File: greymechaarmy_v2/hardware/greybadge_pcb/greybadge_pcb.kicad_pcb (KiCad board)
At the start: 2 copper layers, 75 x 99 mm, 150 parts, among them J1 Conn_02x05_Row_Letter_First, J2 Conn_02x05_Row_Letter_First, J3 Conn_02x05_Row_Letter_First, J4 JST PH S2B, J5 USB_C_Receptacle_USB2.0, Q1 2N7002, Q2 Q_NMOS_GSD, SW1 SW_Push, SW10 SW_Push, SW2 SW_Push, SW3 SW_Push, SW4 SW_Push, SW5 SW_Push, SW6 SW_Push, SW7 SW_Push, SW8 SW_SPDT, SW9 SW_Push, U10 AMS1117-3.3, U2 TLV73311PDBV, U3 TLV73325PDBV, U4 GC9A01_IPS_display, U5 BQ24075, U6 W25Q128JVS, U7 RP2350_60QFN, U8 ECP5U_25_CABGA256, U9 W25Q128JVSIM, X1 SiT2001B, Y1 12Mhz

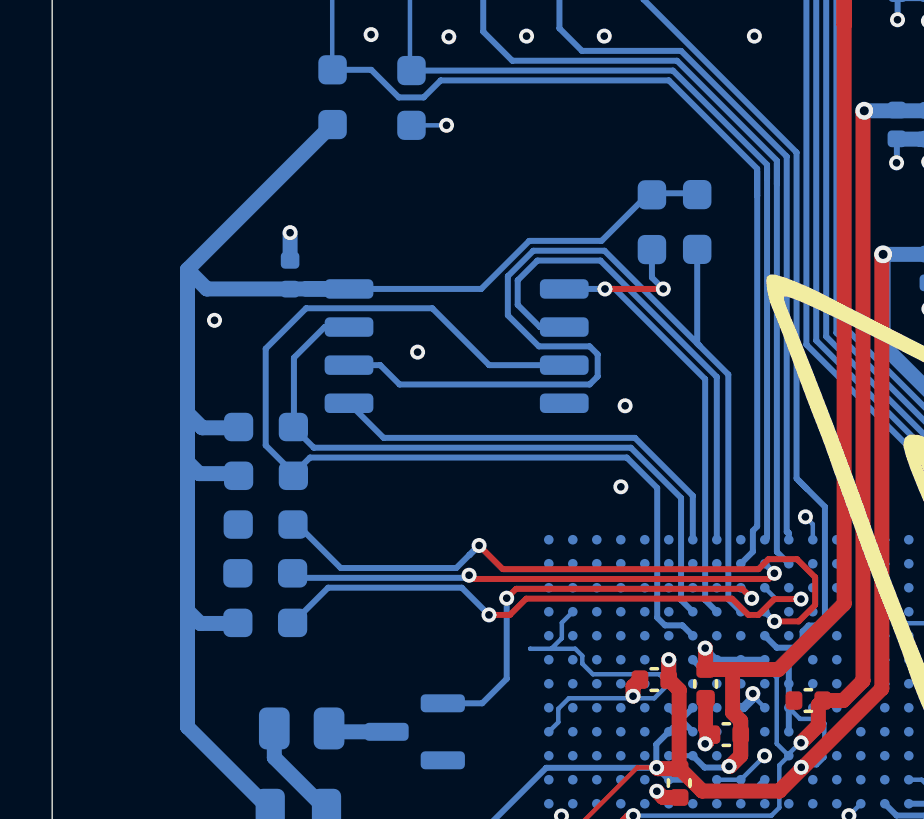
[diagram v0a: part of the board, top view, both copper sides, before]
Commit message: fix: spi flash pinout
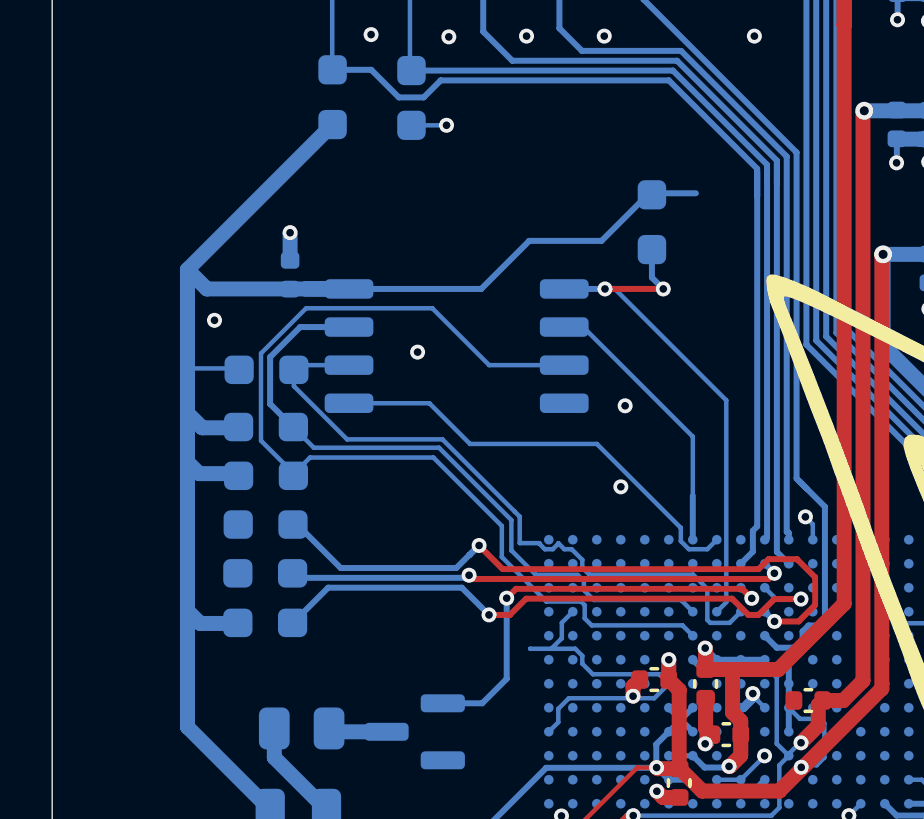
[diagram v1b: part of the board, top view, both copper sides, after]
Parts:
- moved R40 15.2 mm to (88.9, 76.3), turned to 180 degrees
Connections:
- U9 pad 2: sdo -> sdi
- U9 pad 5: sdi -> sdo
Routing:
- net sd_clk: track 35.0 -> 22.2 mm
- net sdi: track 14.2 -> 9.23 mm
- net sdo: track 16.6 -> 14.7 mm
- net +3V3: track 363.3 -> 365.1 mm
- net sd_io2: track 34.4 -> 32.8 mm

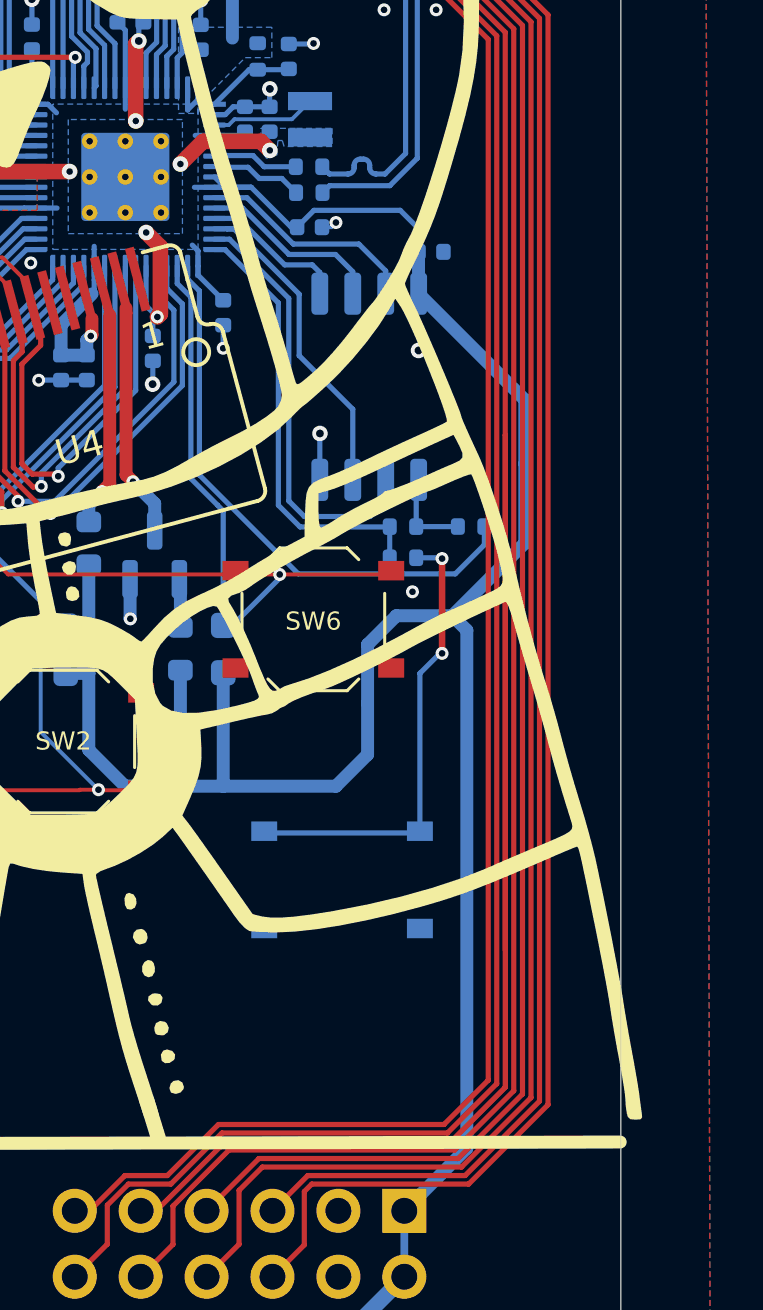
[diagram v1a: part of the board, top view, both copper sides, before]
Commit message: feat: greymecha psram addition in PCB
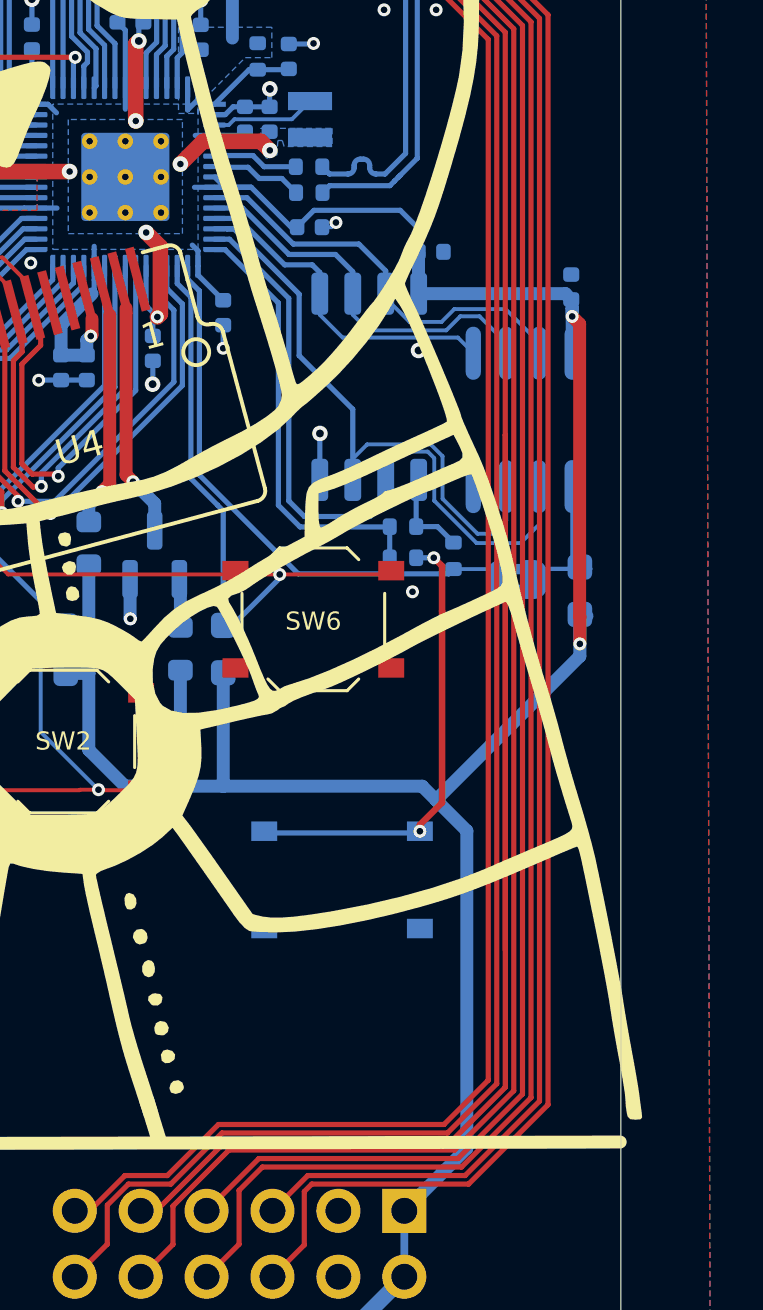
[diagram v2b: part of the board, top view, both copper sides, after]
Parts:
- added C44: 100n, Capacitor_SMD:C_0402_1005Metric, B.Cu at (154.8, 101.6)
- added JP10: SolderJumper_2_Bridged, Jumper:SolderJumper-2_P1.3mm_Bridged2Bar_RoundedPad1.0x1.5mm, B.Cu at (152.8, 112.9)
- added R16: 10k, Resistor_SMD:R_0603_1608Metric_Pad0.98x0.95mm_HandSolder, B.Cu at (155.2, 113.3)
- added U1: APS6404L-3SQR-SN_C5333729, easyeda2kicad:SOIC-8_L4.9-W3.9-P1.27-LS6.0-BL, B.Cu at (153.0, 106.7)
- moved R28 1.32 mm to (150.3, 112.0), turned to 90 degrees
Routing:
- net /rp2350/QSPI_SD1: track 16.7 -> 27.7 mm
- net /rp2350/QSPI_SD2: track 12.5 -> 23.4 mm
- net /rp2350/QSPI_SCLK: track 7.19 -> 15.2 mm
- net /rp2350/QSPI_SD3: track 8.64 -> 16.3 mm
- net /rp2350/QSPI_SD0: track 5.74 -> 13.1 mm
- net Net-(JP10-B): track 0.00 -> 6.03 mm
- net +3V3: track 365.1 -> 368.0 mm, vias 7 -> 9

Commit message: flash rerouting
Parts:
- moved C44 17.0 mm to (150.2, 117.9), turned to -90 degrees
- moved R16 10.6 mm to (146.8, 119.9)
- moved JP10 10.2 mm to (144.3, 118.7)
- moved U1 9.50 mm to (147.6, 114.6), turned to 90 degrees
- moved C36 8.78 mm to (151.4, 108.8)
- moved R29 7.49 mm to (142.1, 106.7), turned to -90 degrees
- moved R28 6.68 mm to (144.2, 109.3)
- moved R32 6.53 mm to (142.6, 108.9)
- moved R10 1.29 mm to (141.4, 114.3)
- moved U6 0.59 mm to (147.6, 105.4), turned to 0 degrees
- moved SW9 0.14 mm to (146.0, 124.6)
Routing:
- net GPIO23: track 113.6 -> 89.4 mm
- net /rp2350/QSPI_SD3: track 16.3 -> 30.3 mm
- net /rp2350/QSPI_SCLK: track 15.2 -> 28.8 mm
- net +3V3: track 368.0 -> 356.5 mm, vias 9 -> 8
- net /rp2350/QSPI_SD0: track 13.1 -> 23.1 mm
- net /rp2350/QSPI_SD1: track 27.7 -> 19.9 mm
- net /rp2350/QSPI_SS: track 17.0 -> 9.78 mm
- net /rp2350/~{USB_BOOT}: track 17.8 -> 24.8 mm
- net /rp2350/QSPI_SD2: track 23.4 -> 20.5 mm
- net Net-(JP10-B): track 6.03 -> 4.10 mm
- net C12: track 71.2 -> 69.3 mm
- net GPIO25: track 82.3 -> 83.6 mm
- net GPIO24: track 87.1 -> 88.4 mm
- net GPIO22: track 88.2 -> 89.5 mm
- net GPIO28: track 81.6 -> 82.8 mm
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
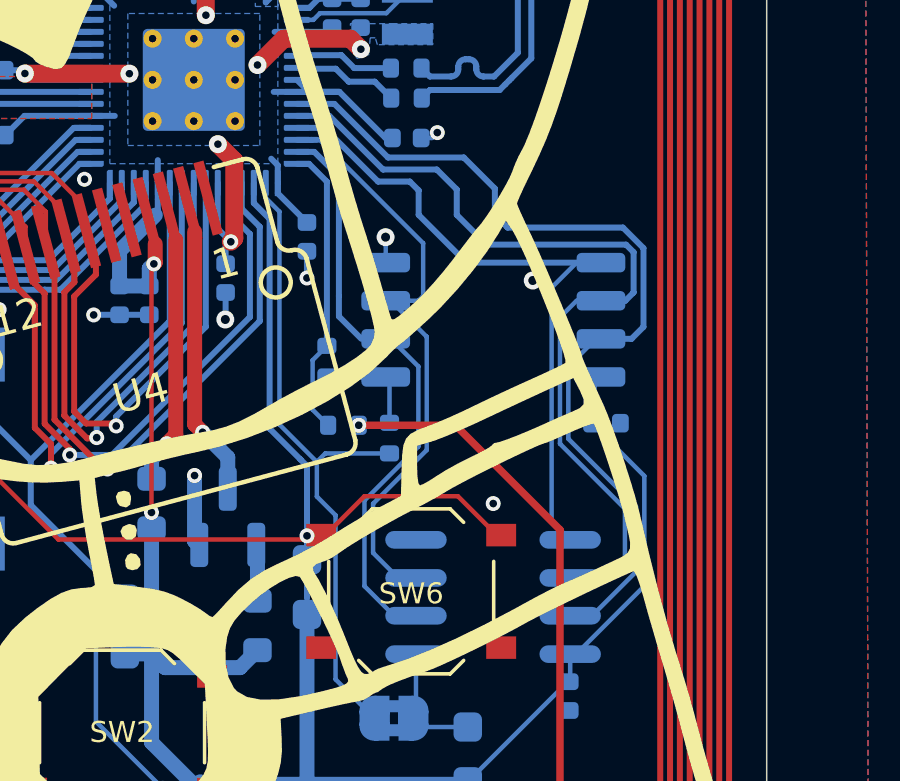
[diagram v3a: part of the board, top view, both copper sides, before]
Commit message: feat: reroute flash for better efficiency
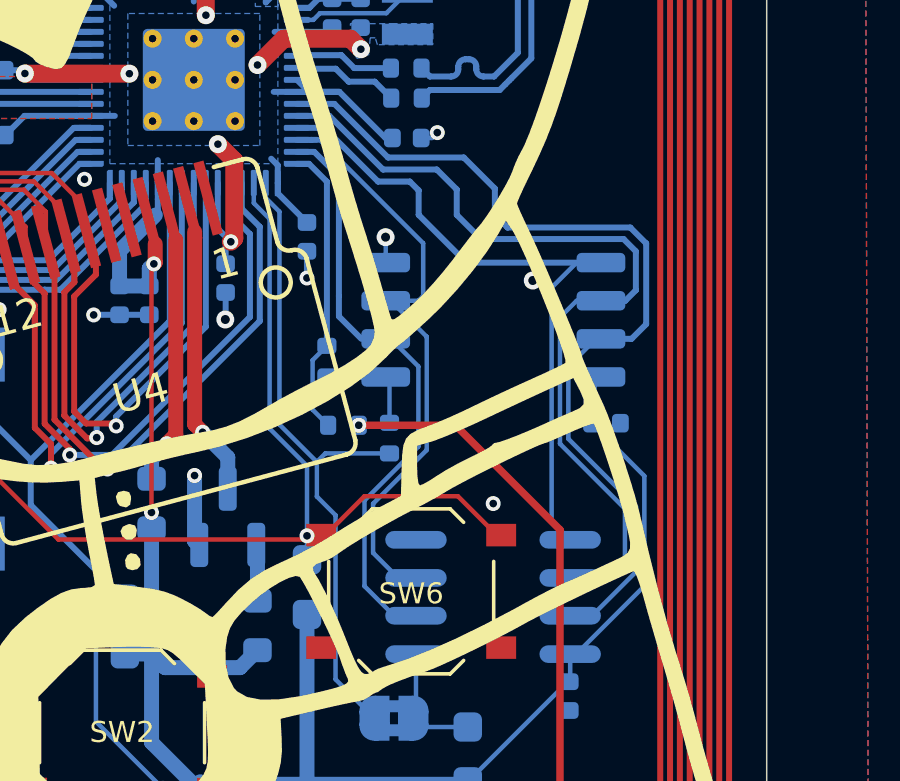
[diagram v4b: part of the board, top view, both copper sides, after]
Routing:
- net C12: track 69.3 -> 68.0 mm
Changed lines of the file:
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@@
 	)
 	(segment
-		(start 151.956905 102.293891)
-		(end 152.642325 102.979311)
+		(start 142.340002 98.171471)
+		(end 144.127503 99.958972)
 		(width 0.2)
 		(layer "B.Cu")
@@
 	)
 	(segment
-		(start 150.929665 115.232993)
-		(end 150.199665 115.232993)
-		(width 0.15)
-		(layer "B.Cu")
-		(net 18)
-	)
-	(segment
-		(start 152.39261 111.590452)
-		(end 152.39261 113.770048)
-		(width 0.15)
+		(start 152.244218 106.003809)
+		(end 151.225825 106.003809)
+		(width 0.2)
 		(layer "B.Cu")
 		(net 18)
 	)
 	(segment
-		(start 151.058689 106.003809)
-		(end 150.137325 106.925173)
-		(width 0.15)
+		(start 147.688631 100.993972)
+		(end 147.688631 101.871472)
+		(width 0.2)
 		(layer "B.Cu")
 		(net 18)
 	)
 	(segment
-		(start 152.39261 113.770048)
-		(end 150.929665 115.232993)
-		(width 0.15)
+		(start 144.127503 99.958972)
+		(end 146.653631 99.958972)
+		(width 0.2)
 		(layer "B.Cu")
 		(net 18)
 	)
 	(segment
-		(start 152.244218 106.003809)
-		(end 151.225825 106.003809)
+		(start 147.688631 101.871472)
+		(end 148.11105 102.293891)
 		(width 0.2)
 		(layer "B.Cu")
@@
 	)
 	(segment
-		(start 147.688631 101.871472)
-		(end 148.11105 102.293891)
-		(width 0.2)
+		(start 150.929665 115.232993)
+		(end 150.199665 115.232993)
+		(width 0.15)
 		(layer "B.Cu")
 		(net 18)
 	)
 	(segment
-		(start 150.137325 109.335167)
-		(end 152.39261 111.590452)
+		(start 152.39261 111.590452)
+		(end 152.39261 113.770048)
 		(width 0.15)
 		(layer "B.Cu")
@@
 	)
 	(segment
-		(start 146.653631 99.958972)
-		(end 147.688631 100.993972)
-		(width 0.2)
+		(start 151.058689 106.003809)
+		(end 150.137325 106.925173)
+		(width 0.15)
 		(layer "B.Cu")
 		(net 18)
 	)
 	(segment
-		(start 152.642325 105.605702)
-		(end 152.244218 106.003809)
-		(width 0.2)
+		(start 152.39261 113.770048)
+		(end 150.929665 115.232993)
+		(width 0.15)
 		(layer "B.Cu")
 		(net 18)
 	)
 	(segment
-		(start 147.688631 100.993972)
-		(end 147.688631 101.871472)
+		(start 152.733593 102.822308)
+		(end 152.733593 105.514434)
 		(width 0.2)
 		(layer "B.Cu")
@@
 	)
 	(segment
-		(start 142.340002 98.171471)
-		(end 144.127503 99.958972)
-		(width 0.2)
+		(start 150.137325 109.335167)
+		(end 152.39261 111.590452)
+		(width 0.15)
 		(layer "B.Cu")
 		(net 18)
 	)
 	(segment
-		(start 152.642325 102.979311)
-		(end 152.642325 105.605702)
+		(start 148.11105 102.293891)
+		(end 152.205176 102.293891)
 		(width 0.2)
 		(layer "B.Cu")
@@
 	)
 	(segment
-		(start 144.127503 99.958972)
-		(end 146.653631 99.958972)
+		(start 152.205176 102.293891)
+		(end 152.733593 102.822308)
 		(width 0.2)
 		(layer "B.Cu")
@@
 	)
 	(segment
-		(start 148.11105 102.293891)
-		(end 151.956905 102.293891)
+		(start 146.653631 99.958972)
+		(end 147.688631 100.993972)
+		(width 0.2)
+		(layer "B.Cu")
+		(net 18)
+	)
+	(segment
+		(start 152.733593 105.514434)
+		(end 152.244218 106.003809)
 		(width 0.2)
 		(layer "B.Cu")
@@
 	)
 	(segment
-		(start 146.418631 101.023972)
-		(end 146.418631 101.871472)
-		(width 0.2)
+		(start 151.487185 113.972993)
+		(end 152.023773 113.436405)
+		(width 0.15)
 		(layer "B.Cu")
 		(net 20)
 	)
 	(segment
-		(start 151.487185 113.972993)
-		(end 152.023773 113.436405)
-		(width 0.15)
+		(start 145.754631 100.359972)
+		(end 146.418631 101.023972)
+		(width 0.2)
 		(layer "B.Cu")
 		(net 20)
 	)
 	(segment
-		(start 147.409968 102.862809)
-		(end 152.061961 102.862809)
+		(start 143.961403 100.359972)
+		(end 145.754631 100.359972)
 		(width 0.2)
 		(layer "B.Cu")
@@
 	)
 	(segment
-		(start 145.754631 100.359972)
-		(end 146.418631 101.023972)
-		(width 0.2)
+		(start 152.023773 111.664928)
+		(end 149.859325 109.50048)
+		(width 0.15)
 		(layer "B.Cu")
 		(net 20)
 	)
 	(segment
-		(start 152.038324 104.733809)
-		(end 151.225825 104.733809)
-		(width 0.2)
+		(start 149.859325 109.50048)
+		(end 149.859325 105.28781)
+		(width 0.15)
 		(layer "B.Cu")
 		(net 20)
 	)
 	(segment
-		(start 152.023773 111.664928)
-		(end 149.859325 109.50048)
+		(start 150.413326 104.733809)
+		(end 151.225825 104.733809)
 		(width 0.15)
 		(layer "B.Cu")
@@
 	)
 	(segment
-		(start 152.314325 104.457808)
-		(end 152.038324 104.733809)
+		(start 152.389629 103.086895)
+		(end 152.389629 104.382504)
 		(width 0.2)
 		(layer "B.Cu")
@@
 	)
 	(segment
-		(start 149.859325 109.50048)
-		(end 149.859325 105.28781)
-		(width 0.15)
+		(start 141.091131 98.571472)
+		(end 142.172903 98.571472)
+		(width 0.2)
 		(layer "B.Cu")
 		(net 20)
 	)
 	(segment
-		(start 146.418631 101.871472)
-		(end 147.409968 102.862809)
-		(width 0.2)
+		(start 149.859325 105.28781)
+		(end 150.413326 104.733809)
+		(width 0.15)
 		(layer "B.Cu")
 		(net 20)
 	)
 	(segment
-		(start 150.413326 104.733809)
-		(end 151.225825 104.733809)
-		(width 0.15)
+		(start 152.389629 104.382504)
+		(end 152.038324 104.733809)
+		(width 0.2)
 		(layer "B.Cu")
 		(net 20)
 	)
 	(segment
-		(start 152.061961 102.862809)
-		(end 152.314325 103.115173)
+		(start 146.418631 101.871472)
+		(end 147.223943 102.676784)
 		(width 0.2)
 		(layer "B.Cu")
@@
 	)
 	(segment
-		(start 141.091131 98.571472)
-		(end 142.172903 98.571472)
+		(start 151.979518 102.676784)
+		(end 152.389629 103.086895)
 		(width 0.2)
 		(layer "B.Cu")
@@
 	)
 	(segment
-		(start 149.859325 105.28781)
-		(end 150.413326 104.733809)
-		(width 0.15)
+		(start 147.223943 102.676784)
+		(end 151.979518 102.676784)
+		(width 0.2)
 		(layer "B.Cu")
 		(net 20)
 	)
 	(segment
-		(start 152.314325 103.115173)
-		(end 152.314325 104.457808)
+		(start 146.418631 101.023972)
+		(end 146.418631 101.871472)
 		(width 0.2)
 		(layer "B.Cu")
@@
 	)
 	(segment
-		(start 143.961403 100.359972)
-		(end 145.754631 100.359972)
+		(start 152.038324 104.733809)
+		(end 151.225825 104.733809)
 		(width 0.2)
 		(layer "B.Cu")
@@
 	)
 	(segment
-		(start 140.180631 108.994493)
-		(end 141.208769 110.022631)
-		(width 0.2)
+		(start 141.4272 110.241062)
+		(end 141.4272 113.366541)
+		(width 0.15)
 		(layer "B.Cu")
 		(net 117)
@@
 	)
 	(segment
-		(start 106.743853 92.723573)
-		(end 107.103599 92.363827)
+		(start 140.180631 108.994493)
+		(end 141.4272 110.241062)
 		(width 0.15)
 		(layer "B.Cu")
@@
 	)
 	(segment
-		(start 141.208769 110.022631)
-		(end 141.4272 110.241062)
-		(width 0.2)
+		(start 106.743853 92.723573)
+		(end 107.103599 92.363827)
+		(width 0.15)
 		(layer "B.Cu")
 		(net 117)
 	)
 	(segment
-		(start 140.180631 102.005972)
+		(start 139.653631 100.808971)
 		(end 139.653631 101.478972)
-		(width 0.2)
+		(width 0.15)
 		(layer "B.Cu")
 		(net 117)
@@
 	(segment
 		(start 139.653631 101.478972)
-		(end 139.653631 100.808971)
-		(width 0.2)
-		(layer "B.Cu")
-		(net 117)
-	)
-	(segment
-		(start 105.906642 92.801274)
-		(end 105.88989 92.784522)
+		(end 140.180631 102.005972)
 		(width 0.15)
 		(layer "B.Cu")
@@
 	)
 	(segment
-		(start 141.4272 110.241062)
-		(end 141.4272 114.6556)
-		(width 0.2)
+		(start 140.180631 102.005972)
+		(end 140.180631 108.994493)
+		(width 0.15)
 		(layer "B.Cu")
 		(net 117)
 	)
 	(segment
-		(start 140.180631 108.994493)
-		(end 140.180631 102.005972)
-		(width 0.2)
+		(start 105.906642 92.801274)
+		(end 105.88989 92.784522)
+		(width 0.15)
 		(layer "B.Cu")
 		(net 117)
